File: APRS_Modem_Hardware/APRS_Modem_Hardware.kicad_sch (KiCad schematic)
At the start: 29 parts, among them U1 LM741, U2 LM386

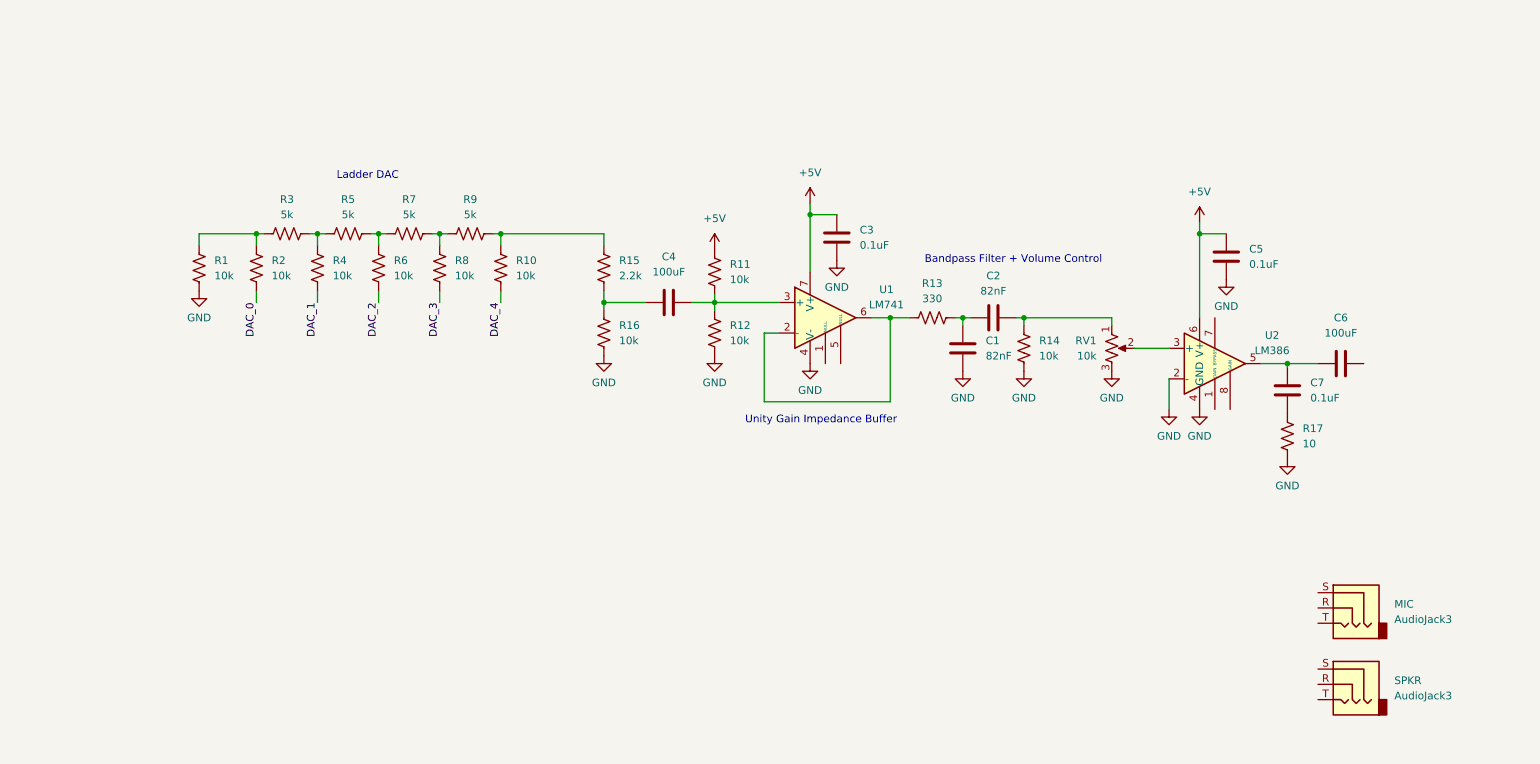
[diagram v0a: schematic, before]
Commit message: update schematic
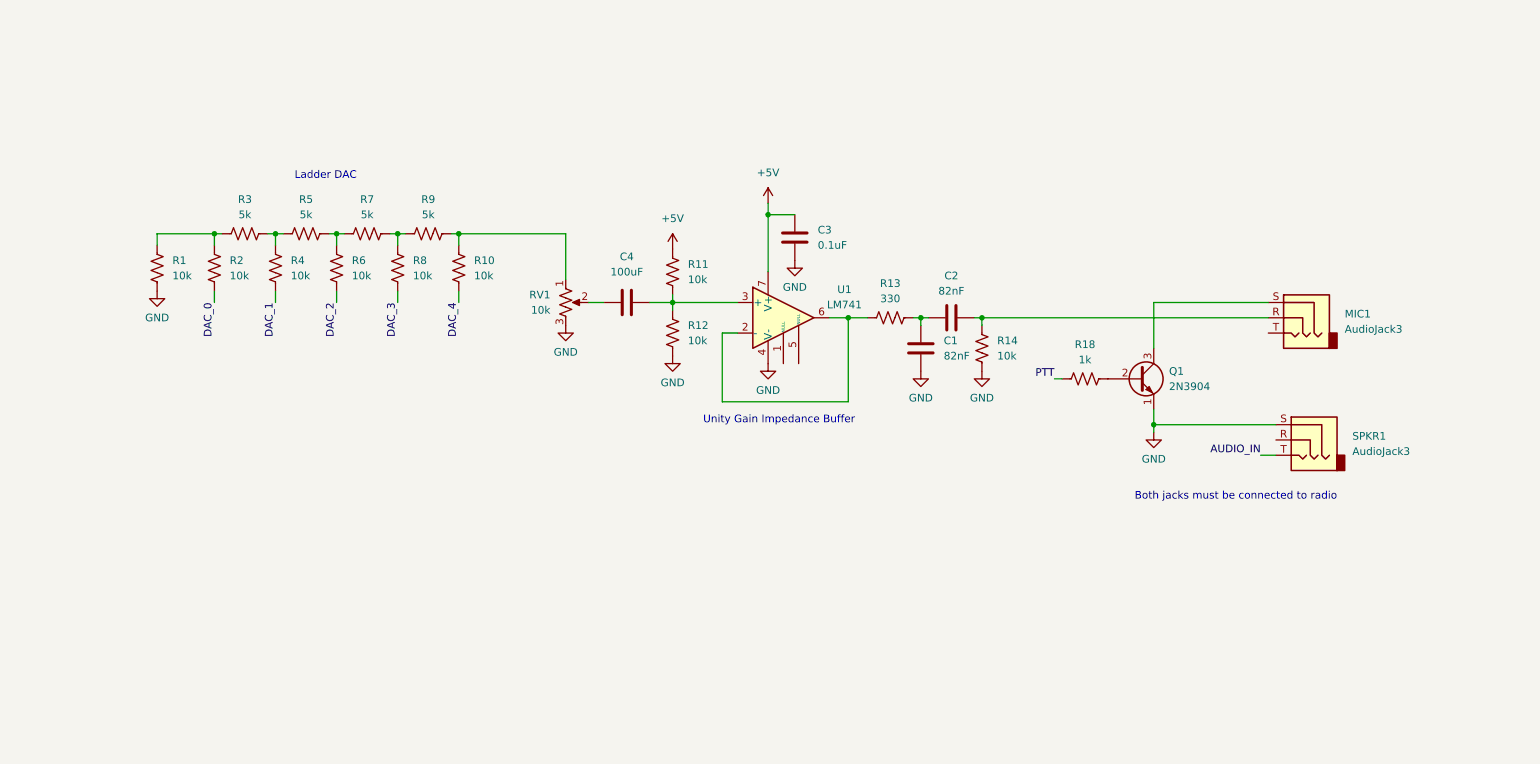
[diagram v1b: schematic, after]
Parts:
- removed C5, C7: 0.1uF, symbol Device:C
- removed C6: 100uF, symbol Device:C
- removed R15: 2.2k, symbol Device:R_US
- removed R16: 10k, symbol Device:R_US
- removed R17: 10, symbol Device:R_US
- removed U2: LM386, symbol Amplifier_Audio:LM386
- added Q1: 2N3904, Package_TO_SOT_THT:TO-92_Inline, symbol Transistor_BJT:2N3904
- added R18: 1k, symbol Device:R_US
- renumbered MIC to MIC1, SPKR to SPKR1
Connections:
- net GND: now also SPKR1.S, Q1.1 (E)
- net at R10.1, R9.2: now also RV1.1
- net at C2.2, R14.1: now also MIC1.R; no longer RV1.1
- net at RV1.2: now also C4.1
- net AUDIO_IN: now reaches SPKR1.T
- net at MIC1.S: now also Q1.3 (C)
- new net: Q1.2 (B), R18.2
- new net PTT: R18.1
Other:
- note added: "Both jacks must be connected to radio"
- note removed: "Bandpass Filter + Volume Control"
- moved on the sheet: C1, C2, C3, C4, MIC1, R1, R10, R11, R12, R13, R14, R2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

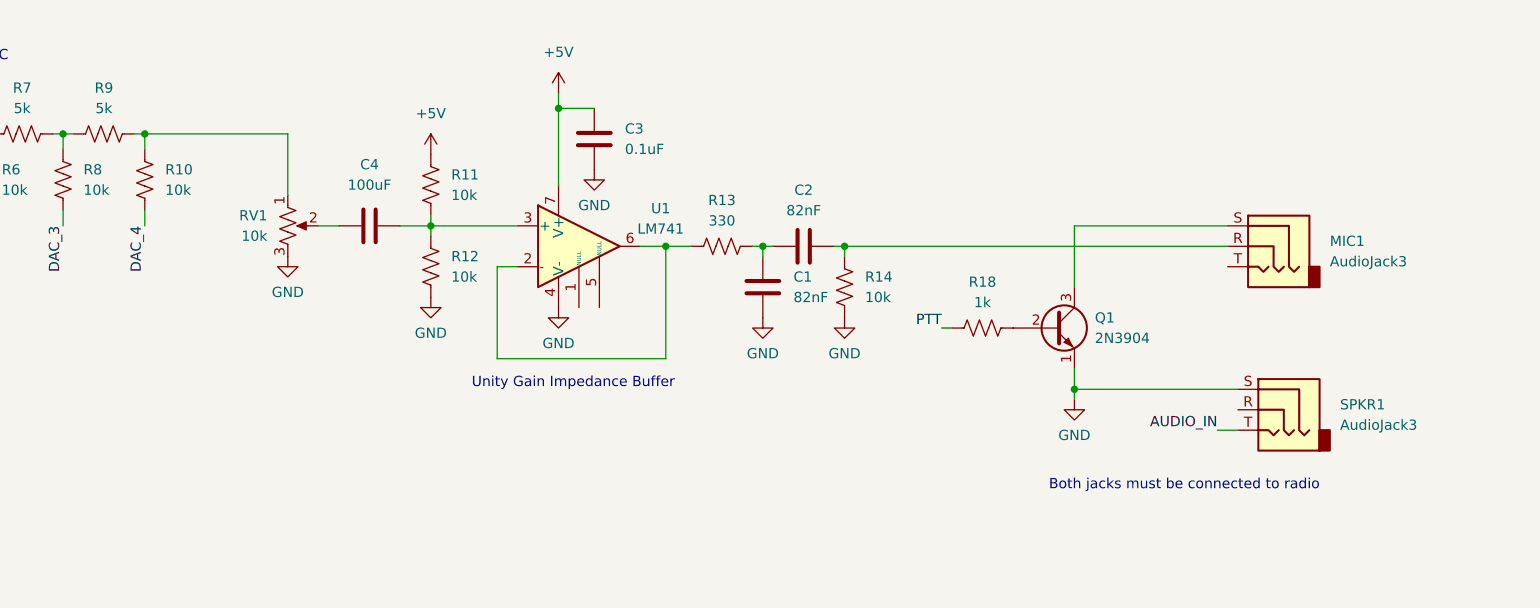
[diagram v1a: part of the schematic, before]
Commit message: update schematic
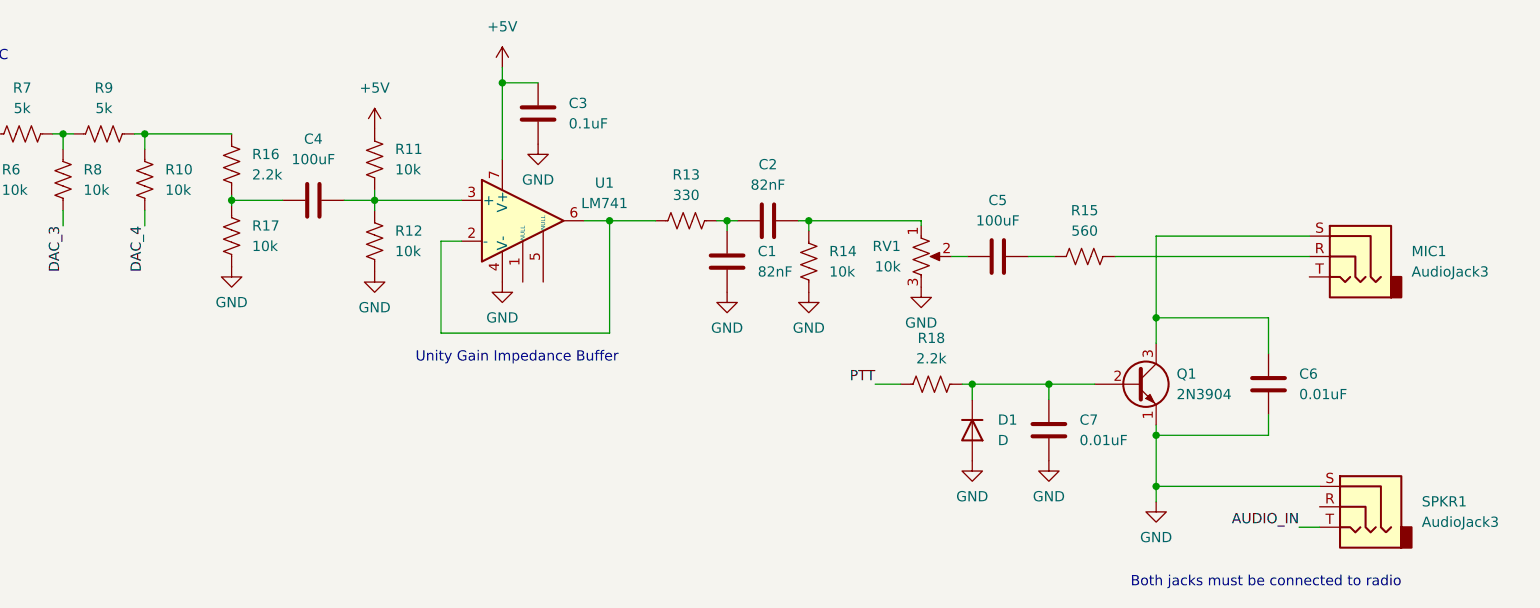
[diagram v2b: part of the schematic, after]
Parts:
- added C5: 100uF, symbol Device:C
- added C6, C7: 0.01uF, symbol Device:C
- added D1: D, symbol Device:D
- added R15: 560, symbol Device:R_US
- added R16: 2.2k, symbol Device:R_US
- added R17: 10k, symbol Device:R_US
- R18: value 1k -> 2.2k
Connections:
- net GND: now also C6.2, C7.2, D1.2 (A), R17.2
- net at R10.1, R9.2: now also R16.1; no longer RV1.1
- net at RV1.2: now also C5.1; no longer C4.1
- net at Q1.2 (B), R18.2: now also C7.1, D1.1 (K)
- net at C2.2, R14.1: now also RV1.1; no longer MIC1.R
- net at MIC1.S, Q1.3 (C): now also C6.1
- new net: C4.1, R16.2, R17.1
- new net: C5.2, R15.1
- new net: MIC1.R, R15.2
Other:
- moved on the sheet: C1, C2, C3, C4, MIC1, Q1, R11, R12, R13, R14, R18, SPKR1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

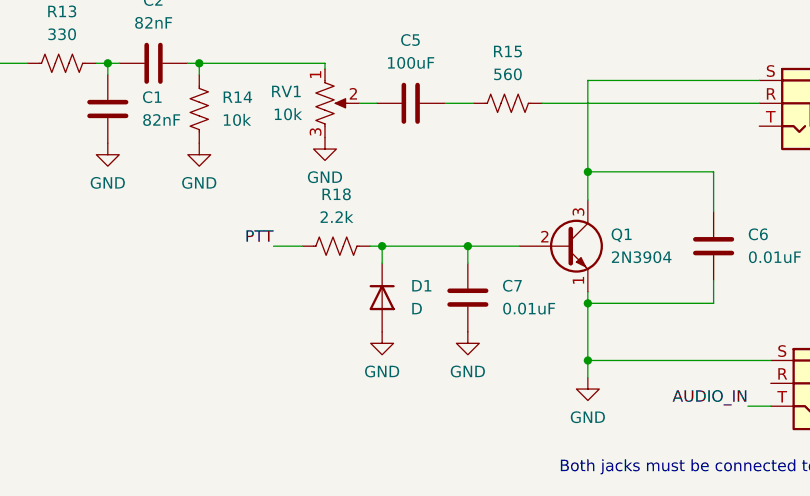
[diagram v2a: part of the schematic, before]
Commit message: update readme and remove useless code
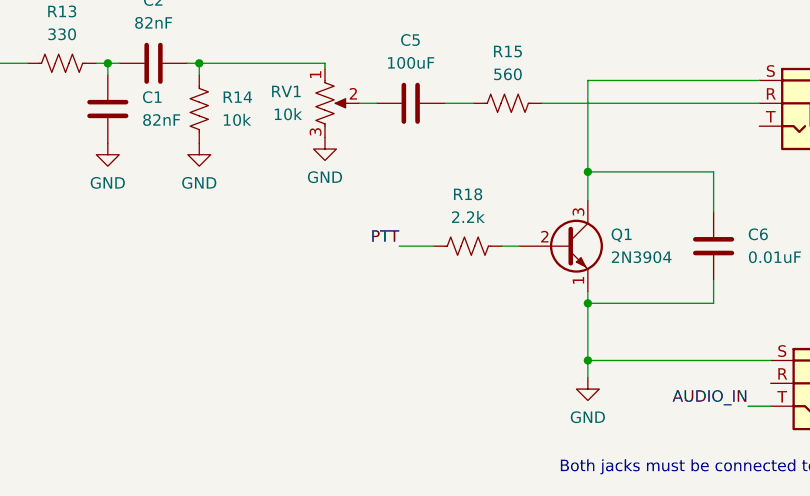
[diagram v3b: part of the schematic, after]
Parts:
- removed C7: 0.01uF, symbol Device:C
- removed D1: D, symbol Device:D
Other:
- moved on the sheet: R18
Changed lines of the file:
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@@
   (junction (at 65.405 72.39) (diameter 0) (color 0 0 0 0)
   )
-  (junction (at 208.28 103.505) (diameter 0) (color 0 0 0 0)
-  )
   (junction (at 153.67 83.185) (diameter 0) (color 0 0 0 0)
   )
-  (junction (at 198.755 103.505) (diameter 0) (color 0 0 0 0)
-  )
   (junction (at 85.725 72.39) (diameter 0) (color 0 0 0 0)
   )
@@
     (stroke (width 0) (type default) (color 0 0 0 0))
   )
-  (wire (pts (xy 186.69 103.505) (xy 189.865 103.505))
+  (wire (pts (xy 200.66 103.505) (xy 204.47 103.505))
     (stroke (width 0) (type default) (color 0 0 0 0))
   )
@@
     (stroke (width 0) (type default) (color 0 0 0 0))
   )
-  (wire (pts (xy 198.755 103.505) (xy 198.755 105.41))
-    (stroke (width 0) (type default) (color 0 0 0 0))
-  )
   (wire (pts (xy 235.585 107.315) (xy 235.585 109.855))
     (stroke (width 0) (type default) (color 0 0 0 0))
@@
     (stroke (width 0) (type default) (color 0 0 0 0))
   )
-  (wire (pts (xy 208.28 103.505) (xy 208.28 105.41))
-    (stroke (width 0) (type default) (color 0 0 0 0))
-  )
   (wire (pts (xy 221.615 108.585) (xy 221.615 109.855))
     (stroke (width 0) (type default) (color 0 0 0 0))
@@
     (stroke (width 0) (type default) (color 0 0 0 0))
   )
-  (wire (pts (xy 198.755 103.505) (xy 208.28 103.505))
-    (stroke (width 0) (type default) (color 0 0 0 0))
-  )
   (wire (pts (xy 221.615 95.25) (xy 235.585 95.25))
     (stroke (width 0) (type default) (color 0 0 0 0))
@@
     (stroke (width 0) (type default) (color 0 0 0 0))
   )
-  (wire (pts (xy 208.28 103.505) (xy 213.995 103.505))
-    (stroke (width 0) (type default) (color 0 0 0 0))
-  )
   (wire (pts (xy 106.68 80.645) (xy 113.03 80.645))
     (stroke (width 0) (type default) (color 0 0 0 0))
@@
     (stroke (width 0) (type default) (color 0 0 0 0))
   )
-  (wire (pts (xy 197.485 103.505) (xy 198.755 103.505))
+  (wire (pts (xy 212.09 103.505) (xy 213.995 103.505))
     (stroke (width 0) (type default) (color 0 0 0 0))
   )
@@
     (effects (font (size 1.27 1.27)) (justify right bottom))
   )
-  (label "PTT" (at 186.69 103.505 180)
+  (label "PTT" (at 200.66 103.505 180)
     (effects (font (size 1.27 1.27)) (justify right bottom))
   )
@@
     (pin "2")
   )
-  (symbol (lib_id "Device:R_US") (at 193.675 103.505 90) (unit 1)
-    (in_bom yes) (on_board yes) (fields_autoplaced)
-    (property "Reference" "R18" (id 0) (at 193.675 97.79 90))
-    (property "Value" "2.2k" (id 1) (at 193.675 100.33 90))
-    (property "Footprint" "" (id 2) (at 193.929 102.489 90)
-      (effects (font (size 1.27 1.27)) hide)
-    )
-    (property "Datasheet" "~" (id 3) (at 193.675 103.505 0)
+  (symbol (lib_id "Device:R_US") (at 208.28 103.505 90) (unit 1)
+    (in_bom yes) (on_board yes) (fields_autoplaced)
+    (property "Reference" "R18" (id 0) (at 208.28 97.79 90))
+    (property "Value" "2.2k" (id 1) (at 208.28 100.33 90))
+    (property "Footprint" "" (id 2) (at 208.534 102.489 90)
+      (effects (font (size 1.27 1.27)) hide)
+    )
+    (property "Datasheet" "~" (id 3) (at 208.28 103.505 0)
       (effects (font (size 1.27 1.27)) hide)
     )
@@
     )
     (property "Datasheet" "" (id 3) (at 221.615 118.11 0)
-      (effects (font (size 1.27 1.27)) hide)
-    )
-    (pin "1")
-  )
-  (symbol (lib_id "power:GND") (at 198.755 113.03 0) (unit 1)
-    (in_bom yes) (on_board yes) (fields_autoplaced)
-    (property "Reference" "#PWR010" (id 0) (at 198.755 119.38 0)
-      (effects (font (size 1.27 1.27)) hide)
-    )
-    (property "Value" "GND" (id 1) (at 198.755 117.475 0))
-    (property "Footprint" "" (id 2) (at 198.755 113.03 0)
-      (effects (font (size 1.27 1.27)) hide)
-    )
-    (property "Datasheet" "" (id 3) (at 198.755 113.03 0)
       (effects (font (size 1.27 1.27)) hide)
     )
@@
     )
     (pin "1")
-  )
-  (symbol (lib_id "Device:D") (at 198.755 109.22 270) (unit 1)
-    (in_bom yes) (on_board yes)
-    (property "Reference" "D1" (id 0) (at 201.93 107.9499 90)
-      (effects (font (size 1.27 1.27)) (justify left))
-    )
-    (property "Value" "D" (id 1) (at 201.93 110.4899 90)
-      (effects (font (size 1.27 1.27)) (justify left))
-    )
-    (property "Footprint" "" (id 2) (at 198.755 109.22 0)
-      (effects (font (size 1.27 1.27)) hide)
-    )
-    (property "Datasheet" "~" (id 3) (at 198.755 109.22 0)
-      (effects (font (size 1.27 1.27)) hide)
-    )
-    (pin "1")
-    (pin "2")
   )
   (symbol (lib_id "Device:R_US") (at 163.195 83.185 90) (unit 1)
@@
     (pin "2")
   )
-  (symbol (lib_id "power:GND") (at 208.28 113.03 0) (unit 1)
-    (in_bom yes) (on_board yes) (fields_autoplaced)
-    (property "Reference" "#PWR012" (id 0) (at 208.28 119.38 0)
-      (effects (font (size 1.27 1.27)) hide)
-    )
-    (property "Value" "GND" (id 1) (at 208.28 117.475 0))
-    (property "Footprint" "" (id 2) (at 208.28 113.03 0)
-      (effects (font (size 1.27 1.27)) hide)
-    )
-    (property "Datasheet" "" (id 3) (at 208.28 113.03 0)
-      (effects (font (size 1.27 1.27)) hide)
-    )
-    (pin "1")
-  )
   (symbol (lib_id "Device:R_US") (at 60.325 72.39 90) (unit 1)
     (in_bom yes) (on_board yes) (fields_autoplaced)
@@
     (pin "2")
   )
-  (symbol (lib_id "Device:C") (at 208.28 109.22 0) (unit 1)
-    (in_bom yes) (on_board yes) (fields_autoplaced)
-    (property "Reference" "C7" (id 0) (at 212.09 107.9499 0)
-      (effects (font (size 1.27 1.27)) (justify left))
-    )
-    (property "Value" "0.01uF" (id 1) (at 212.09 110.4899 0)
-      (effects (font (size 1.27 1.27)) (justify left))
-    )
-    (property "Footprint" "" (id 2) (at 209.2452 113.03 0)
-      (effects (font (size 1.27 1.27)) hide)
-    )
-    (property "Datasheet" "~" (id 3) (at 208.28 109.22 0)
-      (effects (font (size 1.27 1.27)) hide)
-    )
-    (pin "1")
-    (pin "2")
-  )
   (sheet_instances
     (path "/" (page "1"))
@@
       (reference "#PWR09") (unit 1) (value "GND") (footprint "")
     )
-    (path "/25668cc8-3255-4814-b233-656ddb1fd3b2"
-      (reference "#PWR010") (unit 1) (value "GND") (footprint "")
-    )
     (path "/632a28c8-811a-451e-8412-065ea3222ad6"
       (reference "#PWR011") (unit 1) (value "GND") (footprint "")
     )
-    (path "/f0950fdc-4288-4a47-bd2d-66daef84274c"
-      (reference "#PWR012") (unit 1) (value "GND") (footprint "")
-    )
     (path "/23fcd90a-cf28-458c-a47c-15786939988d"
       (reference "#PWR016") (unit 1) (value "GND") (footprint "")
@@
       (reference "C6") (unit 1) (value "0.01uF") (footprint "")
     )
-    (path "/fcd8f6a6-da02-44f4-ac90-b7c9a68e70e7"
-      (reference "C7") (unit 1) (value "0.01uF") (footprint "")
-    )
-    (path "/66efea4d-add0-4856-8135-fd4ed01f8b67"
-      (reference "D1") (unit 1) (value "D") (footprint "")
-    )
     (path "/a8649797-7109-4fea-b9a9-fa81426d5e2f"
